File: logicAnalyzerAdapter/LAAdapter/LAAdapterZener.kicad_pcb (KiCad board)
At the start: 2 copper layers, 13 parts, among them J1 Conn_01x02_Male, J10 Conn_01x01_Female, J2 Conn_01x02_Male, J3 Conn_01x02_Male, J4 Conn_01x02_Male, J5 Conn_02x05_Odd_Even, J6 Conn_01x02_Male, J7 Conn_01x02_Male, J8 Conn_01x02_Male, J9 Conn_01x01_Female

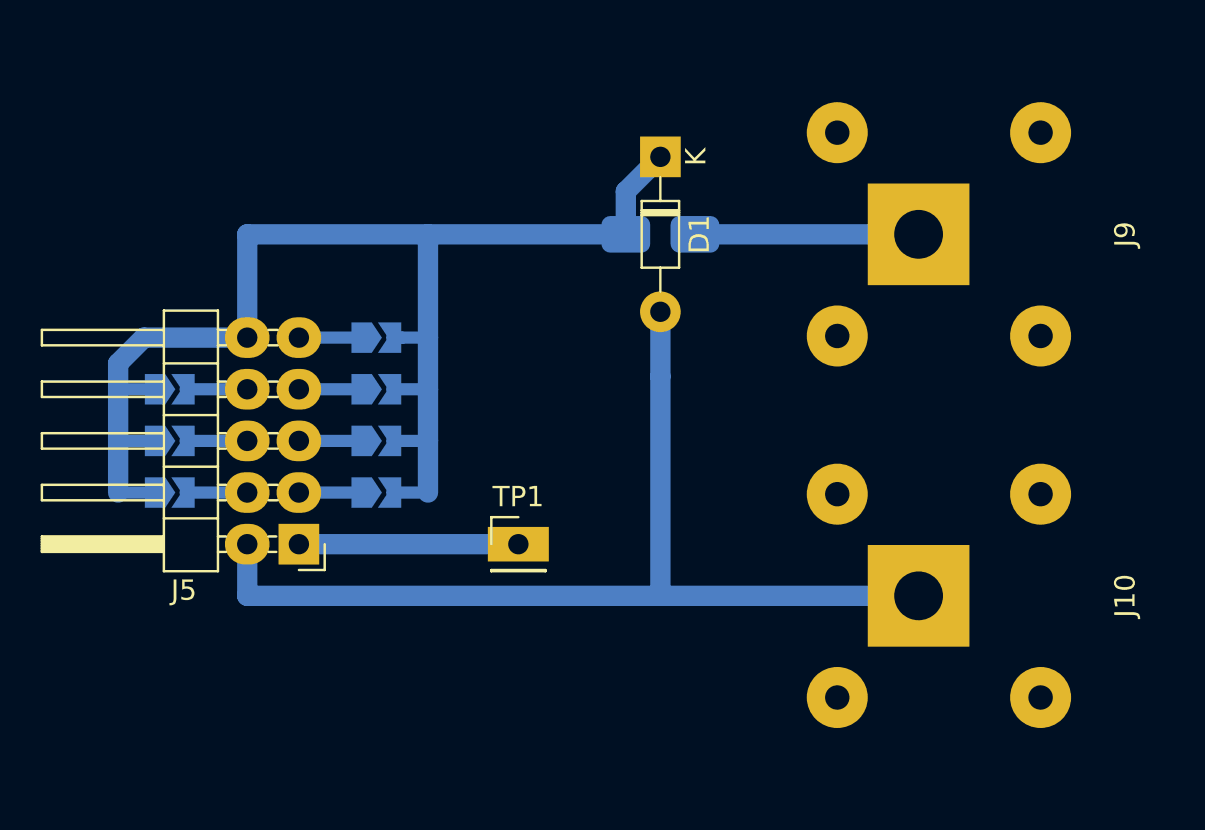
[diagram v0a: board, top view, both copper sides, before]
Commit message: opravena hrubá chyba
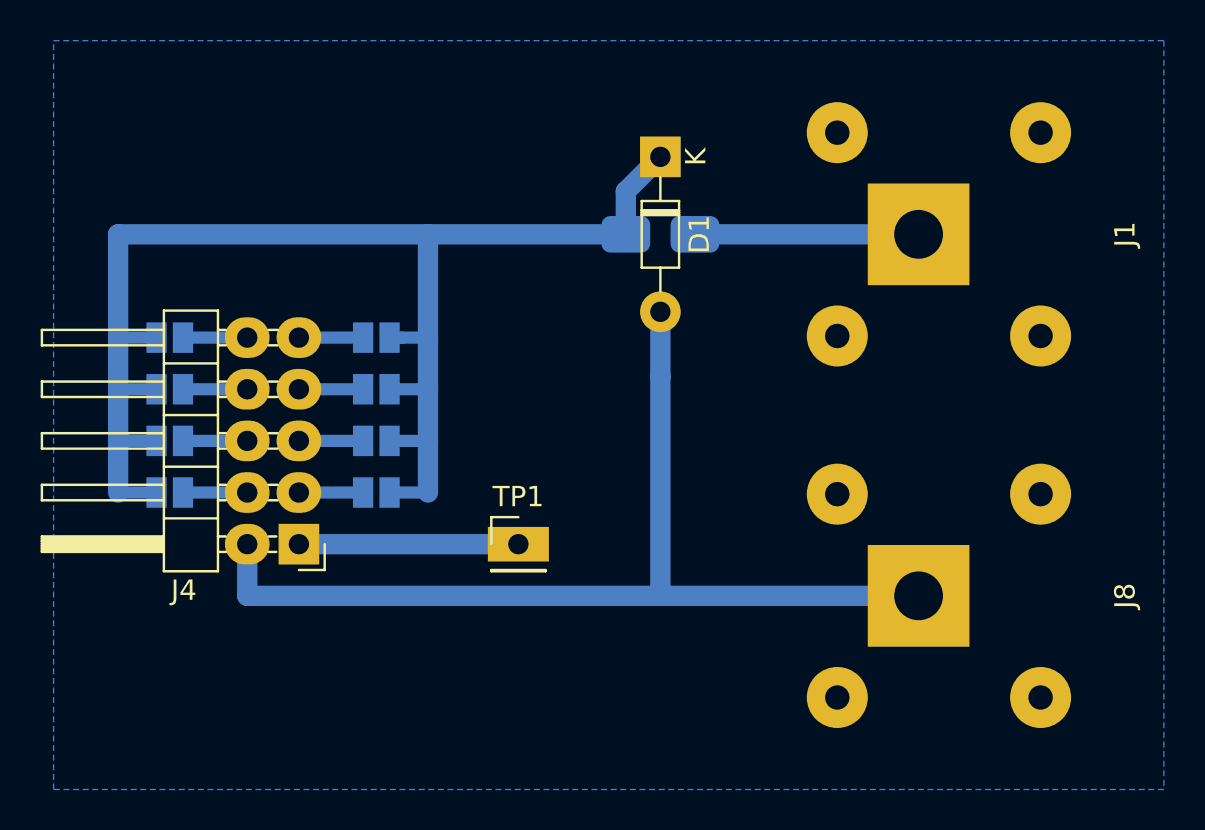
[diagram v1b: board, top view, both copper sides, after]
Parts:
- added J11: Conn_01x02_Male, Jumper:SolderJumper-2_P1.3mm_Open_Pad1.0x1.5mm, B.Cu at (156.8, 85.7)
- J10: renamed from J6; footprint Jumper:SolderJumper-2_P1.3mm_Open_TrianglePad1.0x1.5mm -> Jumper:SolderJumper-2_P1.3mm_Open_Pad1.0x1.5mm
- J2: renamed from J1; footprint Jumper:SolderJumper-2_P1.3mm_Open_TrianglePad1.0x1.5mm -> Jumper:SolderJumper-2_P1.3mm_Open_Pad1.0x1.5mm
- J3: renamed from J2; footprint Jumper:SolderJumper-2_P1.3mm_Open_TrianglePad1.0x1.5mm -> Jumper:SolderJumper-2_P1.3mm_Open_Pad1.0x1.5mm
- J5: renamed from J8; footprint Jumper:SolderJumper-2_P1.3mm_Open_TrianglePad1.0x1.5mm -> Jumper:SolderJumper-2_P1.3mm_Open_Pad1.0x1.5mm
- J6: renamed from J3; footprint Jumper:SolderJumper-2_P1.3mm_Open_TrianglePad1.0x1.5mm -> Jumper:SolderJumper-2_P1.3mm_Open_Pad1.0x1.5mm
- J7: footprint Jumper:SolderJumper-2_P1.3mm_Open_TrianglePad1.0x1.5mm -> Jumper:SolderJumper-2_P1.3mm_Open_Pad1.0x1.5mm
- J9: renamed from J4; footprint Jumper:SolderJumper-2_P1.3mm_Open_TrianglePad1.0x1.5mm -> Jumper:SolderJumper-2_P1.3mm_Open_Pad1.0x1.5mm
- renumbered J9 to J1, J5 to J4, J10 to J8
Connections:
- J4 pad 10: Net-(D1-Pad1) -> Net-(J11-Pad1)
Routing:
- net Net-(J11-Pad1): track 0.00 -> 3.16 mm
- net Net-(D1-Pad1): track 66.6 -> 69.3 mm
- added copper zone on B.Cu, net Net-(D1-Pad2)
